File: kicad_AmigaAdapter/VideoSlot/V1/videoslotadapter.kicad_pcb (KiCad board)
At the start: 2 copper layers, 152 x 57.6 mm, 18 parts, among them J1 A2000 Video Slot Edge Connect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, U1 74LVC86, U2 74LVC574, U3 74LVC574, U4 TLV74333PDBVR, U5 74LVC86

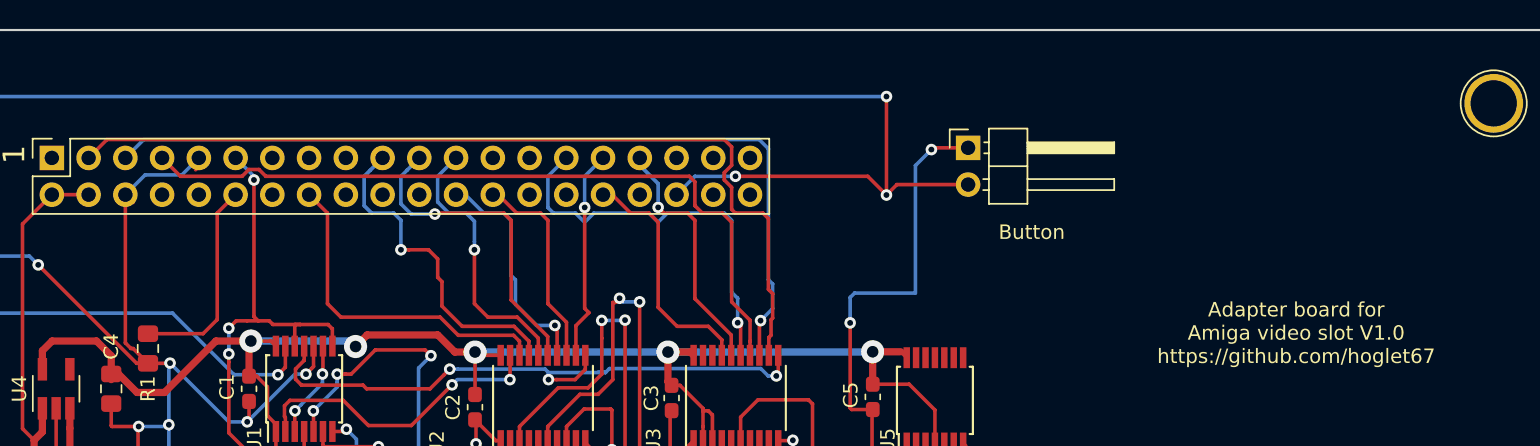
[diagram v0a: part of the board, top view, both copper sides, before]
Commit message: V1.01 layout updates to inlcude 47pf capacitor, ground extra floating pins on U5
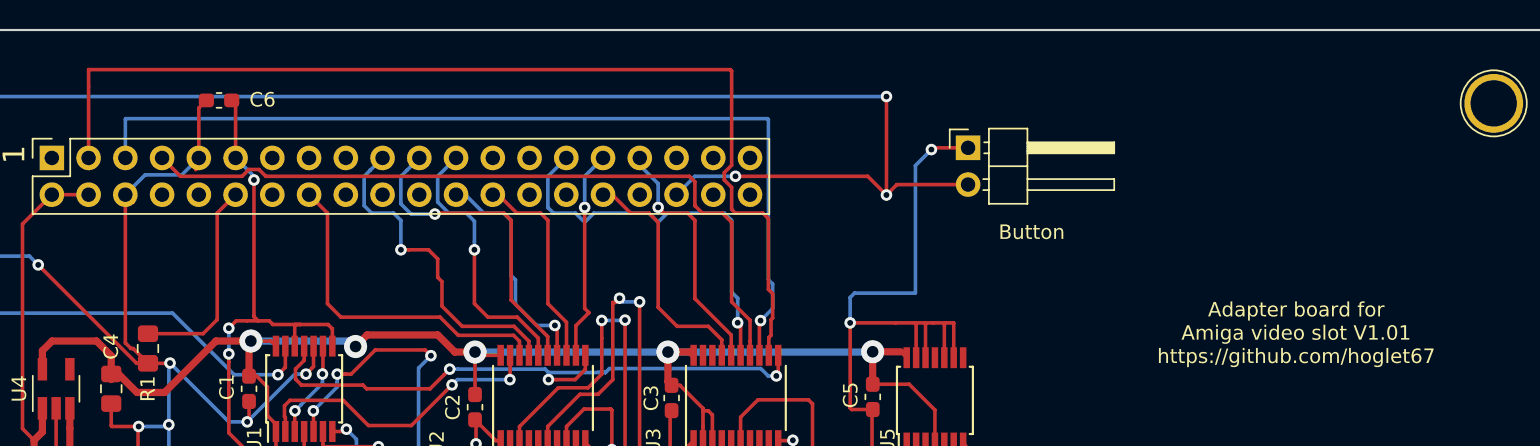
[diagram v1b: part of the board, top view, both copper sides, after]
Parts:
- added C6: 47pf, Capacitor_SMD:C_0603_1608Metric_Pad1.05x0.95mm_HandSolder, F.Cu at (148.1, 64.3)
- renumbered JButton1 to JButton2
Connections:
- U5 pad 10: (no net) -> GND
- U5 pad 12: (no net) -> GND
- U5 pad 13: (no net) -> GND
- U5 pad 9: (no net) -> GND
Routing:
- net GND: track 306.3 -> 327.3 mm
- net /PiB0: track 62.4 -> 73.1 mm
- net /PiCLK: track 51.3 -> 55.4 mm
- net /PiB1: track 60.0 -> 64.0 mm
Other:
- board text added: "Adapter board for Amiga video slot V1.01 https://github.com/hoglet67"
- board text removed: "Adapter board for Amiga video slot V1.0 https://github.com/hoglet67"

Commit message: V1.1 Updates to improve picture quality and eliminate the need for excessive overclocking
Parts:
- removed C5: 100nF, Capacitor_SMD:C_0603_1608Metric_Pad1.05x0.95mm_HandSolder
- removed C6: 47pf, Capacitor_SMD:C_0603_1608Metric_Pad1.05x0.95mm_HandSolder
- removed U5: 74LVC86, Housings_SSOP:TSSOP-14_4.4x5mm_Pitch0.65mm
- moved JP1 25.7 mm to (138.8, 101.1)
- moved R1 18.8 mm to (160.7, 74.7), turned to 0 degrees
- moved C1 16.3 mm to (133.9, 85.0)
- moved U1 16.3 mm to (137.7, 85.0)
- moved C4 13.1 mm to (132.6, 74.0)
- moved U4 13.1 mm to (128.8, 74.0)
- moved JRaspberryPiZero1 7.84 mm to (144.4, 68.3)
- moved JButton2 3.44 mm to (119.3, 69.3)
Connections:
- J1 pad 22: (no net) -> GND
- JRaspberryPiZero1 pad 14: Net-(JRaspberryPiZero1-Pad14) -> GND
- JRaspberryPiZero1 pad 20: Net-(JRaspberryPiZero1-Pad20) -> GND
- JRaspberryPiZero1 pad 25: Net-(JRaspberryPiZero1-Pad25) -> GND
- JRaspberryPiZero1 pad 30: Net-(JRaspberryPiZero1-Pad30) -> GND
- JRaspberryPiZero1 pad 34: Net-(JRaspberryPiZero1-Pad34) -> GND
- JRaspberryPiZero1 pad 39: Net-(JRaspberryPiZero1-Pad39) -> GND
- U1 pad 4: +3V3 -> /C1
- U1 pad 5: /7MHZ -> /C3
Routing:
- net GND: track 327.3 -> 60.7 mm, vias 29 -> 23
- net /7MHZ: track 67.1 -> 0.00 mm, vias 6 -> 0
- net /C3: track 86.4 -> 25.5 mm, vias 5 -> 1
- net Net-(JP1-Pad3): track 56.3 -> 8.20 mm, vias 5 -> 0
- net /CDAC: track 45.4 -> 11.3 mm, vias 3 -> 0
- net /PiB0: track 73.1 -> 48.5 mm, vias 0 -> 1
- net +5V: track 129.1 -> 151.2 mm
- net Net-(JButton1-Pad2): track 111.3 -> 92.2 mm, vias 4 -> 0
- net /PiB1: track 64.0 -> 45.1 mm
- net Net-(JP1-Pad2): track 47.0 -> 28.2 mm, vias 3 -> 1
- net /PiCLK: track 55.4 -> 73.5 mm, vias 3 -> 0
- net /G3: track 48.4 -> 30.6 mm, vias 3 -> 1
- net +3V3: track 106.9 -> 89.4 mm, vias 6 -> 3
- net Net-(U1-Pad2): track 21.3 -> 38.3 mm
- net /PiB3: track 27.8 -> 15.4 mm
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- added copper zone on B.Cu, net GND
- added copper zone on F.Cu, net GND
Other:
- board text added: "Adapter board for Amiga video slot V1.1 https://github.com/hoglet67"
- board text removed: "Adapter board for Amiga video slot V1.01 https://github.com/hoglet67"
